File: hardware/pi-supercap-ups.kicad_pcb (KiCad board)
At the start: 2 copper layers, 65 x 56 mm, 89 parts, among them J1 Screw_Terminal_01x04, J2 Raspberry_Pi_2_3, J3 Conn_01x08_Male, J4 Conn_01x02_Male, U1 ATtiny25-20SU, U2 MCP2515-xSO, U3 TJA1051T-3, U5 MP1584EN, U6 MT3608, U7 MT9700, Y1 8MHz

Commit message: Layout partially done before change of plans
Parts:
- removed C3, C4, C5, C6: 10F, custom:CP_Radial_D10.0mm_P5.00mm_flat
- removed D10: GLED, LED_SMD:LED_0603_1608Metric_Pad1.05x0.95mm_HandSolder
- removed D13, D14, D15: DS34W, Diode_SMD:D_SOD-123F
- removed D6: RLED, LED_SMD:LED_0603_1608Metric_Pad1.05x0.95mm_HandSolder
- removed D8, D9: ZMM55C2V7, Diode_SMD:D_MiniMELF_Handsoldering
- removed R21: 2.2k, Resistor_SMD:R_0603_1608Metric_Pad1.05x0.95mm_HandSolder
- removed R24, R25, R26: 0, Resistor_SMD:R_0603_1608Metric_Pad1.05x0.95mm_HandSolder
- removed R29: 10k, Resistor_SMD:R_0603_1608Metric_Pad1.05x0.95mm_HandSolder
- removed R4: 1.5k, Resistor_SMD:R_0603_1608Metric_Pad1.05x0.95mm_HandSolder
- removed TP4: Vcap, TestPoint:TestPoint_Keystone_5000-5004_Miniature
- added C12: 10nF 5V, Capacitor_SMD:C_0603_1608Metric_Pad1.05x0.95mm_HandSolder, F.Cu at (67.8, 70.9)
- added C20: 10uF 10V, Capacitor_SMD:C_0603_1608Metric_Pad1.05x0.95mm_HandSolder, F.Cu at (57.7, 70.1)
- added C21: 10uF 10V, Capacitor_SMD:C_0603_1608Metric_Pad1.05x0.95mm_HandSolder, F.Cu at (57.7, 66.0)
- added C22: 10uF 10V, Capacitor_SMD:C_0603_1608Metric_Pad1.05x0.95mm_HandSolder, F.Cu at (65.0, 70.9)
- added C23: 10uF 10V, Capacitor_SMD:C_0603_1608Metric_Pad1.05x0.95mm_HandSolder, F.Cu at (65.8, 66.3)
- added SW1: SW_SPST, Connector_PinHeader_2.54mm:PinHeader_1x02_P2.54mm_Vertical, F.Cu at (75.7, 71.9)
- added TP3: Vcap, TestPoint:TestPoint_Keystone_5000-5004_Miniature, F.Cu at (45.7, 50.0)
- added U4: TPS61022, custom:TPS61022RWUR, F.Cu at (65.5, 51.1)
- C1: value 47uF -> 47uF 10V
- C13: value 10uF -> 10uF 50V
- C16: value 100uF -> 22uF 6.3V; footprint Capacitor_SMD:C_1210_3225Metric_Pad1.42x2.65mm_HandSolder -> Capacitor_SMD:C_0603_1608Metric_Pad1.05x0.95mm_HandSolder
- C17: value 100uF -> 100uF 10V
- C18: value 100nF -> 10nF 10V
- C19: value 22uF -> 1uF 10V; footprint Capacitor_SMD:C_0805_2012Metric_Pad1.15x1.40mm_HandSolder -> Capacitor_SMD:C_0603_1608Metric_Pad1.05x0.95mm_HandSolder
- D4: value RLED -> BAT54C; footprint Diode_SMD:D_0603_1608Metric_Pad1.05x0.95mm_HandSolder -> Package_TO_SOT_SMD:SOT-23
- D7: value BAT54S -> GLED; footprint Package_TO_SOT_SMD:SOT-23 -> LED_SMD:LED_0603_1608Metric_Pad1.05x0.95mm_HandSolder
- J1: footprint custom:15EDGVC-3.81-4P -> custom:WJ2EDGR-5.08-4P
- J3: value Conn_01x08_Male -> Conn_02x07_Counter_Clockwise; footprint Connector_PinHeader_2.54mm:PinHeader_2x04_P2.54mm_Vertical -> custom:PinHeader_2x07_P2.54mm_Vertical_CounterClockwise
- J4: footprint Connector_PinHeader_2.54mm:PinHeader_1x02_P2.54mm_Vertical -> custom:WJ2EDGR-5.08-2P
- L1: value 15uH -> 10uH 3.5A; footprint CSAB0630-100M:INDC6060X300 -> custom:L_TDK_SLF10165_HandSolder
- L2: value 5.6uH -> 1uH; footprint Inductor_SMD:L_Taiyo-Yuden_NR-40xx_HandSoldering -> Inductor_SMD:L_Wuerth_HCI-1350
- R12: value 100k -> 200k
- R13: value 100k -> 54.9k
- R14: value 232k -> 93k
- R16: value 110k -> 147k
- R17: value 15k -> 20k
- R18: value 6.8k -> 4.53k
- R2: value 2.2k -> 10k
- R20: value 2.2k -> 100k
- R22: value 0 -> 10k
- R23: value 0 -> 4.53k
- R27: value 4.7k -> 50k
- R9: value 2.2k -> 1.5k
- TP9: value Vboost -> VboostSW
- U1: value ATtiny25-20SU -> ATtiny44-20SSU; footprint Package_SO:SOIJ-8_5.3x5.3mm_P1.27mm -> Package_SO:SOIC-14_3.9x8.7mm_P1.27mm
- U6: value MT3608 -> MT9700; footprint Package_TO_SOT_SMD:SOT-23-6_Handsoldering -> Package_TO_SOT_SMD:SOT-23-5_HandSoldering
- moved D7 57.3 mm to (21.3, 33.5), turned to 90 degrees
- moved R6 42.8 mm to (27.7, 33.9), turned to 180 degrees
- moved R5 41.3 mm to (27.7, 32.0), turned to 180 degrees
- moved R2 36.7 mm to (58.4, 48.5), turned to 0 degrees
- moved D4 34.9 mm to (45.7, 34.0)
- moved L1 32.6 mm to (39.4, 59.9), turned to 90 degrees
- moved C13 32.5 mm to (50.0, 66.3), turned to 90 degrees
- moved C14 32.3 mm to (46.5, 64.5)
- moved R12 31.8 mm to (49.8, 69.8)
- moved U5 31.7 mm to (45.2, 68.3)
- moved C15 30.6 mm to (40.6, 69.3), turned to 270 degrees
- moved R14 30.2 mm to (41.4, 71.9)
- moved R15 30.2 mm to (44.8, 71.9)
- moved R13 29.4 mm to (39.1, 69.3), turned to 90 degrees
- moved R23 29.4 mm to (65.0, 63.2), turned to 90 degrees
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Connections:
- net /inv_Sense_Vcc/+12V renamed /Vin
- C16 pad 1: /Buck converter/Vout -> 2.65V
- C18 pad 1: Net-(C18-Pad1) -> /V12:6
- C2 pad 1: 3.3V -> /ATT_Vcc
- D4 pad 1: GND -> 2.65V
- D4 pad 2: Net-(D4-Pad2) -> 3.3V
- D7 pad 2: 3.3V -> Net-(D7-Pad2)
- J2 pad 15: (no net) -> /INT
- J2 pad 22: /INT -> (no net)
- J2 pad 36: /GPIO16 -> (no net)
- J2 pad 37: /GPIO26 -> (no net)
- J3 pad 1: /ATTiny_RESET -> /ATT_Vcc
- J3 pad 2: /PB3 -> /PB0
- J3 pad 3: /PB4 -> /ATT_LED0
- J3 pad 4: GND -> /ATT_RESET
- J3 pad 5: /PB0 -> /ATT_LED1
- J3 pad 6: /PB1 -> /PA7
- J3 pad 7: /PB2 -> /SDA
- J3 pad 8: 3.3V -> /PA5
- J4 pad 1: /Sense_Vcc -> GND
- J4 pad 2: /Vcap:2 -> /Vcap
- L1 pad 2: /Buck converter/Vout -> 2.65V
- R10 pad 1: /ATTiny_LED -> /ATT_LED0
- R14 pad 2: /Buck converter/Vout -> 2.65V
- R19 pad 1: /Current limiting/Vin -> 2.65V
- R2 pad 1: /Vcap -> /EN5V
- R2 pad 2: Net-(D4-Pad2) -> Net-(R2-Pad2)
- R20 pad 2: /Vcap:2 -> /VcapS
- R22 pad 1: /PB2 -> Net-(R22-Pad1)
- R22 pad 2: /GPIO3 -> GND
- R23 pad 1: /PB1 -> Net-(R23-Pad1)
- R23 pad 2: /GPIO2 -> GND
- R27 pad 2: Net-(C18-Pad1) -> /V12:6
- R28 pad 1: Net-(C18-Pad1) -> /V12:6
- R5 pad 1: /PB4 -> /SDA
- R5 pad 2: /Sense_Vcc -> /GPIO2
- R6 pad 1: /ATTiny_RESET -> /SCL
- R6 pad 2: /GPIO16 -> /GPIO3
- R7 pad 1: 3.3V -> /ATT_Vcc
- R7 pad 2: /ATTiny_RESET -> /ATT_RESET
- R9 pad 1: /CAN_L -> /ATT_LED1
- R9 pad 2: Net-(D10-Pad2) -> Net-(D7-Pad2)
- TP8 pad 1: /5V -> 2.65V
- U1 pad 1: /ATTiny_RESET -> /ATT_Vcc
- U1 pad 2: /PB3 -> /PB0
- U1 pad 3: /PB4 -> /ATT_LED0
- U1 pad 4: GND -> /ATT_RESET
- U1 pad 5: /PB0 -> /ATT_LED1
- U1 pad 6: /PB1 -> /PA7
- U1 pad 7: /PB2 -> /SDA
- U1 pad 8: 3.3V -> /PA5
- U6 pad 1: /Boost converter/SW -> /Vcap
- U6 pad 3: /Boost converter/FB -> Net-(R18-Pad1)
- U6 pad 4: /Vcap -> Net-(R19-Pad2)
- U6 pad 5: /Vcap -> 2.65V
- U7 pad 3: Net-(R18-Pad1) -> Net-(R23-Pad1)
- U7 pad 5: /Current limiting/Vin -> 2.65V
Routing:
- net 2.65V: track 0.00 -> 98.0 mm, vias 0 -> 8
- net /ATTiny_LED: track 56.4 -> 0.00 mm, vias 2 -> 0
- net /VcapS: track 0.00 -> 55.9 mm, vias 0 -> 6
- net 3.3V: track 102.2 -> 54.9 mm, vias 6 -> 5
- net Net-(R2-Pad2): track 0.00 -> 47.2 mm, vias 0 -> 4
- net /ATT_LED1: track 0.00 -> 44.3 mm, vias 0 -> 7
- net /GPIO3: track 57.8 -> 13.6 mm, vias 3 -> 0
- net /GPIO2: track 54.7 -> 10.6 mm, vias 3 -> 0
- net /SDA: track 0.00 -> 43.3 mm, vias 0 -> 6
- net /ATT_LED0: track 0.00 -> 42.8 mm, vias 0 -> 4
- net /Power Bank/Vc1: track 41.7 -> 0.00 mm, vias 2 -> 0
- net /SCL: track 0.00 -> 41.2 mm, vias 0 -> 4
- net /V12:6: track 0.00 -> 37.6 mm, vias 0 -> 4
- net /CANbus interface/TX: track 44.0 -> 7.80 mm, vias 4 -> 0
- net /CAN_L: track 74.1 -> 38.9 mm
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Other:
- board text added: "12V"
- board text added: "5V"
- board text added: "ACT"
- board text added: "PWR"

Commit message: revE ready for production
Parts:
- removed C7, C8: 22pF, Capacitor_SMD:C_0603_1608Metric_Pad1.05x0.95mm_HandSolder
- removed R22: 10k, Resistor_SMD:R_0603_1608Metric_Pad1.05x0.95mm_HandSolder
- removed TP6: RX, TestPoint:TestPoint_Keystone_5000-5004_Miniature
- removed TP7: TX, TestPoint:TestPoint_Keystone_5000-5004_Miniature
- removed TP9: VboostSW, TestPoint:TestPoint_Keystone_5000-5004_Miniature
- removed the U2 at (36.5, 33.4)
- removed U3: TJA1051T-3, Package_SO:SOIC-8_3.9x4.9mm_P1.27mm
- removed Y1: 8MHz, Crystal:Crystal_HC49-U_Vertical
- added BT1: CR1220 3V, custom:BatteryHolder_Linx_BAT-HLD-012-SMT, B.Cu at (78.4, 36.3)
- added C27: 100nF, Capacitor_SMD:C_0603_1608Metric_Pad1.05x0.95mm_HandSolder, F.Cu at (73.4, 27.4)
- added C3: 100nF, Capacitor_SMD:C_0603_1608Metric_Pad1.05x0.95mm_HandSolder, F.Cu at (57.3, 34.4)
- added C4: 100nF, Capacitor_SMD:C_0603_1608Metric_Pad1.05x0.95mm_HandSolder, F.Cu at (61.2, 38.5)
- added C5: 100nF, Capacitor_SMD:C_0603_1608Metric_Pad1.05x0.95mm_HandSolder, F.Cu at (67.4, 31.9)
- added C6: 47uF 10V, Capacitor_SMD:C_1206_3216Metric_Pad1.42x1.75mm_HandSolder, F.Cu at (37.4, 52.7)
- added IC1: MCP25625T-E_ML, custom:QFN65P600X600X100-29M-D, F.Cu at (62.6, 33.4)
- added IC2: MCP25625T-E_ML, custom:QFN65P600X600X100-29M-D, F.Cu at (63.4, 44.6)
- added J5: Screw_Terminal_01x03, custom:TerminalBlock_WJ15EDGRC-3.81-3P, F.Cu at (28.4, 46.7)
- added JP2: Term, Connector_PinHeader_2.54mm:PinHeader_1x02_P2.54mm_Vertical, F.Cu at (32.8, 40.1)
- added R21: 10k, Resistor_SMD:R_0603_1608Metric_Pad1.05x0.95mm_HandSolder, F.Cu at (58.8, 28.4)
- added R24: 10k, Resistor_SMD:R_0603_1608Metric_Pad1.05x0.95mm_HandSolder, F.Cu at (57.3, 31.0)
- added R25: 10k, Resistor_SMD:R_0603_1608Metric_Pad1.05x0.95mm_HandSolder, F.Cu at (64.4, 28.4)
- added R29: 10k, Resistor_SMD:R_0603_1608Metric_Pad1.05x0.95mm_HandSolder, F.Cu at (57.6, 41.0)
- added R30: 10k, Resistor_SMD:R_0603_1608Metric_Pad1.05x0.95mm_HandSolder, F.Cu at (64.8, 38.5)
- added R31: 120R, Resistor_SMD:R_1206_3216Metric_Pad1.42x1.75mm_HandSolder, F.Cu at (35.8, 41.3)
- added R4: 0, Resistor_SMD:R_0603_1608Metric_Pad1.05x0.95mm_HandSolder, F.Cu at (40.4, 32.1)
- added U4: DS3231MZ, Package_SO:SOIC-8_3.9x4.9mm_P1.27mm, F.Cu at (78.1, 31.9)
- added X1: S3D8.000000B20F30T, Oscillator:Oscillator_SMD_Abracon_ASE-4Pin_3.2x2.5mm, F.Cu at (69.1, 36.8)
- C11, C9: value 47uF -> 100nF; footprint Capacitor_SMD:C_0805_2012Metric_Pad1.15x1.40mm_HandSolder -> Capacitor_SMD:C_0603_1608Metric_Pad1.05x0.95mm_HandSolder
- C12: value 10nF 5V -> 100nF
- C17: value 100uF 10V -> 47uF 10V; footprint Capacitor_SMD:C_1210_3225Metric_Pad1.42x2.65mm_HandSolder -> Capacitor_SMD:C_1206_3216Metric_Pad1.42x1.75mm_HandSolder
- C18: value 10nF 10V -> 100nF
- C19: value 1uF 10V -> 10uF 10V
- D3, D5: footprint Diode_SMD:D_0603_1608Metric_Pad1.05x0.95mm_HandSolder -> LED_SMD:LED_0603_1608Metric_Pad1.05x0.95mm_HandSolder
- J1: footprint custom:WJ2EDGR-5.08-4P -> custom:TerminalBlock_WJ15EDGRC-3.81-4P
- J4: value Conn_01x02_Male -> Screw_Terminal_01x02; footprint custom:WJ2EDGR-5.08-2P -> custom:TerminalBlock_WJ15EDGRC-3.81-2P
- L1: footprint custom:L_TDK_SLF10165_HandSolder -> Inductor_SMD:L_Abracon_ASPI-0630LR
- L2: footprint Inductor_SMD:L_Wuerth_HCI-1350 -> Inductor_SMD:L_Abracon_ASPI-0630LR
- R27: value 50k -> 51k
- R8: value 10k -> 0
- moved D11 57.6 mm to (58.7, 73.1), turned to 0 degrees
- moved D7 56.9 mm to (62.3, 73.0), turned to 0 degrees
- moved R10 55.1 mm to (58.7, 71.3), turned to 0 degrees
- moved R9 54.4 mm to (62.3, 71.2), turned to 0 degrees
- moved J4 49.7 mm to (28.6, 60.1), turned to 270 degrees
- moved J1 49.6 mm to (28.6, 29.6), turned to 270 degrees
- moved SW1 46.1 mm to (29.6, 71.9), turned to 90 degrees
- moved TP5 42.0 mm to (70.0, 31.0)
- moved R14 38.6 mm to (79.5, 65.8), turned to 270 degrees
- moved R13 37.9 mm to (77.0, 68.1), turned to 180 degrees
- moved C15 36.4 mm to (77.0, 66.5), turned to 0 degrees
- moved R15 36.0 mm to (79.5, 62.3), turned to 90 degrees
- moved JP1 34.7 mm to (32.8, 32.3)
- moved C17 34.6 mm to (35.1, 52.7), turned to 90 degrees
- moved R17 34.5 mm to (32.5, 58.3), turned to 90 degrees
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- renumbered U4 to U2
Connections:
- C1 pad 1: /5V -> 5V
- C10 pad 1: GND -> 3.3V
- C10 pad 2: 3.3V -> GND
- C11 pad 1: GND -> 5V
- C11 pad 2: /5V -> GND
- C17 pad 1: /5V -> 5V
- J1 pad 1: +12V -> GND
- J1 pad 2: GND -> +12V
- J1 pad 3: /CAN_H -> /CAN0_L
- J1 pad 4: /CAN_L -> /CAN0_H
- J2 pad 13: (no net) -> /GPIO27
- J2 pad 15: /INT -> /GPIO22
- J2 pad 2: /5V -> 5V
- J2 pad 24: /CS -> /CS0
- J2 pad 26: (no net) -> /CS1
- J2 pad 4: /5V -> 5V
- JP1 pad 1: /CAN_L -> /CAN0_L
- R11 pad 2: /CAN_H -> /CAN0_H
- R16 pad 1: /5V -> 5V
- R3 pad 1: /5V -> 5V
- R8 pad 1: 3.3V -> /INT1
- R8 pad 2: Net-(R8-Pad2) -> /GPIO27
- TP5 pad 1: /CANbus interface/OSC1 -> /CANbus interface/OSC_OUT
- U2 pad 3: /5V -> 5V
- U2 pad 6: Net-(R22-Pad1) -> GND
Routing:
- net /5V: track 162.2 -> 0.00 mm, vias 8 -> 0
- net 5V: track 0.00 -> 140.4 mm, vias 0 -> 8
- net +12V: track 11.0 -> 99.7 mm, vias 0 -> 4
- net 3.3V: track 54.9 -> 140.8 mm, vias 5 -> 17
- net /CAN0_H: track 0.00 -> 72.8 mm, vias 0 -> 7
- net /CAN0_L: track 0.00 -> 72.8 mm, vias 0 -> 6
- net /INT1: track 0.00 -> 61.4 mm, vias 0 -> 6
- net /CAN1_L: track 0.00 -> 57.5 mm, vias 0 -> 5
- net /CAN1_H: track 0.00 -> 55.1 mm, vias 0 -> 7
- net GND: track 0.00 -> 52.5 mm, vias 0 -> 149
- net /GPIO2: track 10.6 -> 62.4 mm, vias 0 -> 5
- net /GPIO3: track 13.6 -> 61.5 mm, vias 0 -> 5
- net /CAN_L: track 38.9 -> 0.00 mm, vias 3 -> 0
- net /CAN_H: track 34.6 -> 0.00 mm, vias 4 -> 0
- net /Vin: track 93.1 -> 60.3 mm
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- added copper zone on B.Cu, net (none)
- added copper zone on F.Cu, net 5V
- removed copper zone on B.Cu, net /5V
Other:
- outline, holes or cut-outs redrawn

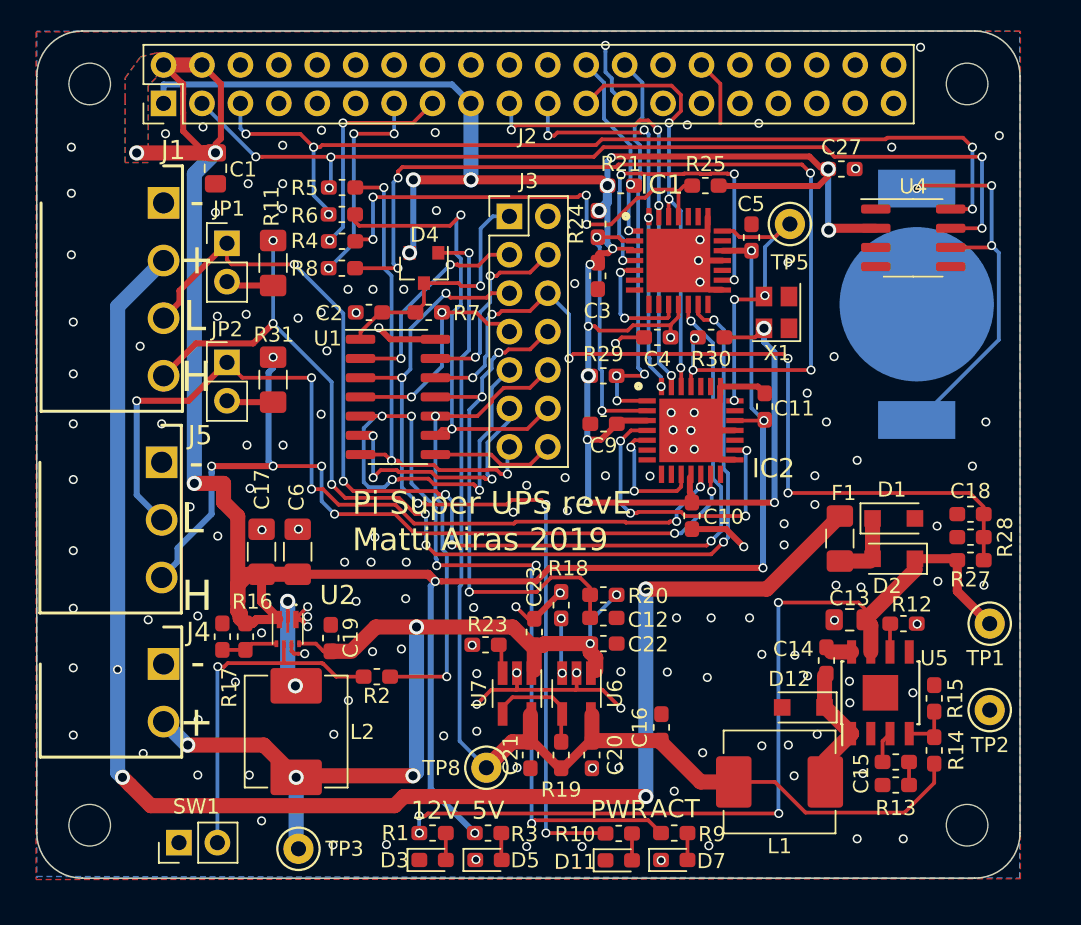
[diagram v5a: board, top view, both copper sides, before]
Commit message: Fixed wrong footprints & passive component values.
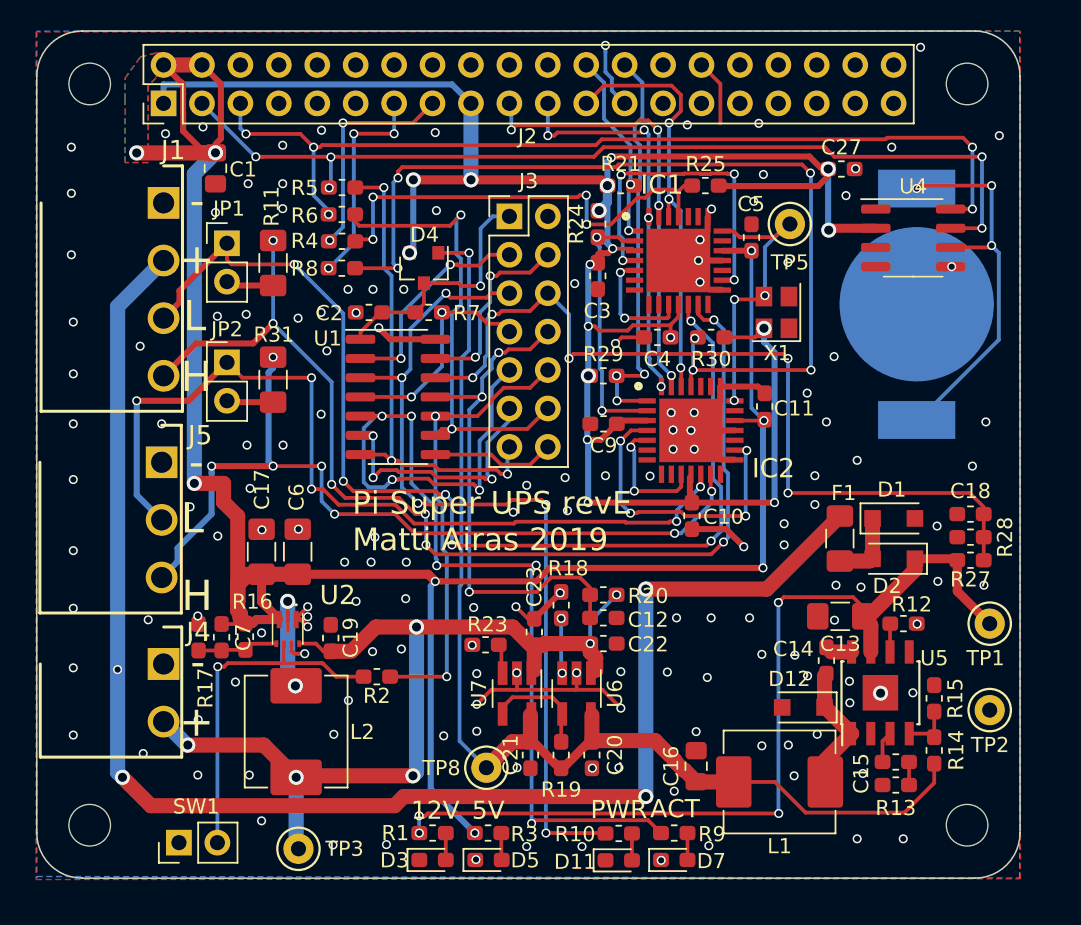
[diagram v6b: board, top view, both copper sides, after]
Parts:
- added C7: 220p, Capacitor_SMD:C_0603_1608Metric_Pad1.05x0.95mm_HandSolder, F.Cu at (32.4, 58.3)
- C13: footprint Capacitor_SMD:C_0805_2012Metric_Pad1.15x1.40mm_HandSolder -> Capacitor_SMD:C_1206_3216Metric_Pad1.42x1.75mm_HandSolder
- C16: value 22uF 6.3V -> 47uF 6.3V; footprint Capacitor_SMD:C_0603_1608Metric_Pad1.05x0.95mm_HandSolder -> Capacitor_SMD:C_0805_2012Metric_Pad1.15x1.40mm_HandSolder
- R16: value 147k -> 330k
- R17: value 20k -> 43k
- moved C16 3.44 mm to (63.8, 66.8)
- moved R17 1.58 mm to (30.9, 58.3)
- moved C13 0.66 mm to (73.3, 56.9)
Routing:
- net 5V: track 140.4 -> 142.0 mm
- net /Boost converter/FB: track 3.74 -> 5.26 mm
- net GND: track 52.5 -> 52.6 mm, vias 149 -> 155

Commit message: Redesign SMPS layouts.
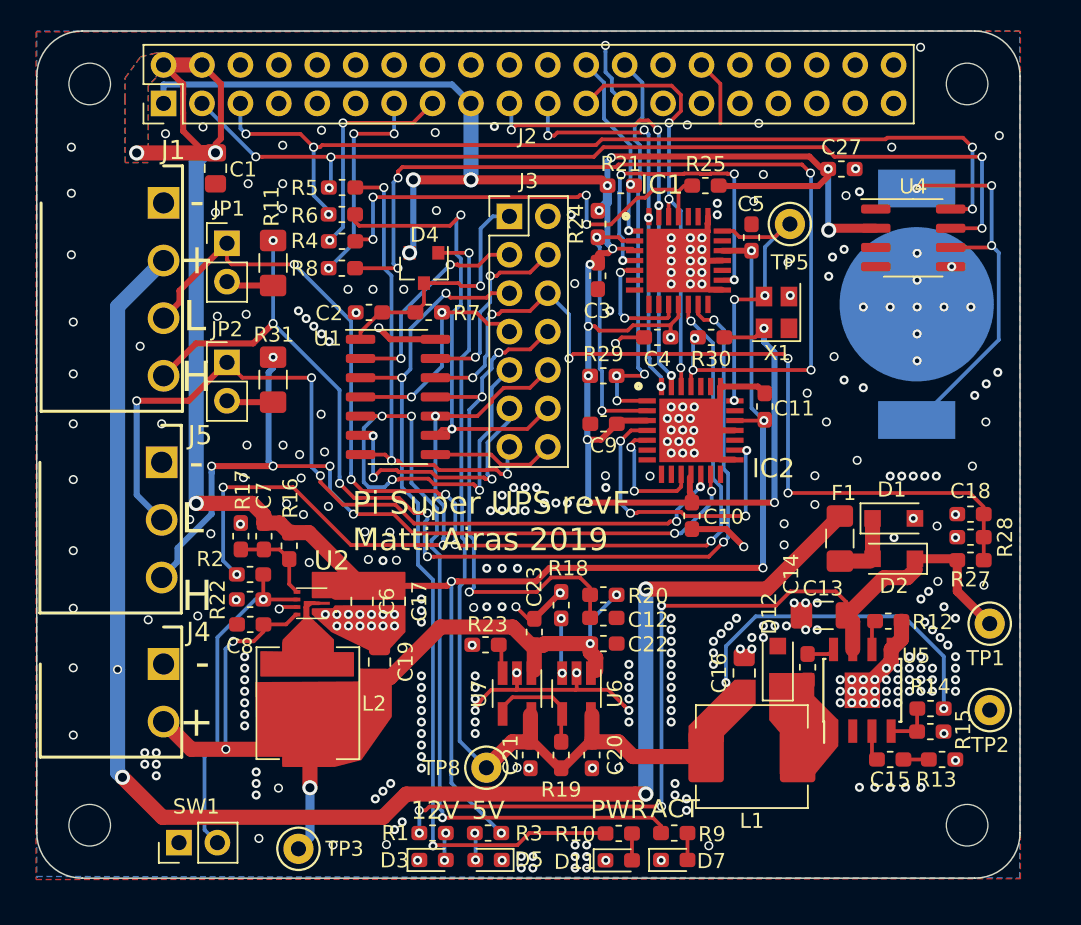
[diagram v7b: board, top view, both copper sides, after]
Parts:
- added C8: 100n, Capacitor_SMD:C_0603_1608Metric_Pad1.05x0.95mm_HandSolder, F.Cu at (34.3, 57.5)
- added R22: 100k, Resistor_SMD:R_0603_1608Metric_Pad1.05x0.95mm_HandSolder, F.Cu at (34.3, 55.8)
- C17, C6: footprint Capacitor_SMD:C_1206_3216Metric_Pad1.42x1.75mm_HandSolder -> Capacitor_SMD:C_0805_2012Metric_Pad1.15x1.40mm_HandSolder
- C19: value 10uF 10V -> 47uF 6.3V; footprint Capacitor_SMD:C_0603_1608Metric_Pad1.05x0.95mm_HandSolder -> Capacitor_SMD:C_0805_2012Metric_Pad1.15x1.40mm_HandSolder
- moved R2 10.8 mm to (34.3, 54.2), turned to 0 degrees
- moved C17 9.37 mm to (43.8, 55.9), turned to 270 degrees
- moved R17 7.24 mm to (33.7, 51.6)
- moved C7 7.24 mm to (35.2, 51.6)
- moved C16 6.93 mm to (67.0, 60.7)
- moved R16 6.67 mm to (36.9, 52.3)
- moved C6 5.37 mm to (41.7, 55.9), turned to 270 degrees
- moved C19 3.59 mm to (42.8, 59.9)
- moved R13 3.49 mm to (80.0, 66.4), turned to 0 degrees
- moved D12 3.15 mm to (69.2, 60.3), turned to 90 degrees
- moved R14 2.78 mm to (79.3, 63.0), turned to 0 degrees
- moved L1 2.48 mm to (67.5, 66.2)
- moved U2 2.33 mm to (38.4, 56.1), turned to 180 degrees
- moved R15 2.21 mm to (79.3, 64.5), turned to 0 degrees
- moved L2 2.03 mm to (38.1, 62.7)
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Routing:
- net GND: track 52.6 -> 71.5 mm, vias 155 -> 336
- net 2.65V: track 75.8 -> 86.9 mm, vias 1 -> 3
- net 5V: track 142.0 -> 131.8 mm
- net /EN5V: track 30.1 -> 39.8 mm, vias 2 -> 4
- net /Boost converter/SW: track 7.21 -> 4.39 mm, vias 2 -> 0
- net /Buck converter/SW: track 7.01 -> 9.64 mm
- net /Vcap: track 60.8 -> 59.7 mm, vias 6 -> 5
- net Net-(R2-Pad2): track 23.0 -> 22.2 mm
- net /Vin: track 60.6 -> 61.4 mm
- net /CAN1_L: track 57.5 -> 56.8 mm
- net /Boost converter/FB: track 5.26 -> 5.85 mm
- net +12V: track 99.7 -> 100.3 mm
- net /ATT_LED1: track 68.9 -> 68.4 mm, vias 7 -> 5
- net /ATT_LED0: track 57.1 -> 57.5 mm, vias 5 -> 3
- net Net-(D3-Pad2): track 1.78 -> 1.94 mm, vias 0 -> 2
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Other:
- board text added: "Pi Super UPS revF Matti Airas 2019"
- board text removed: "Pi Super UPS revE Matti Airas 2019"
